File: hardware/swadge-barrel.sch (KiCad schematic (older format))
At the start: 42 parts, among them J1 USB_B_Micro, SW1 4-1437565-2, SW2 4-1437565-2, SW3 4-1437565-2, SW4 SW_SPDT, U1 ESP-13-WROOM-02D, U2 DISP_OLED_UG-2864HSWEG01, U3 BUS_PCIexpress, U4 QMA6981, U5 AP1117-33

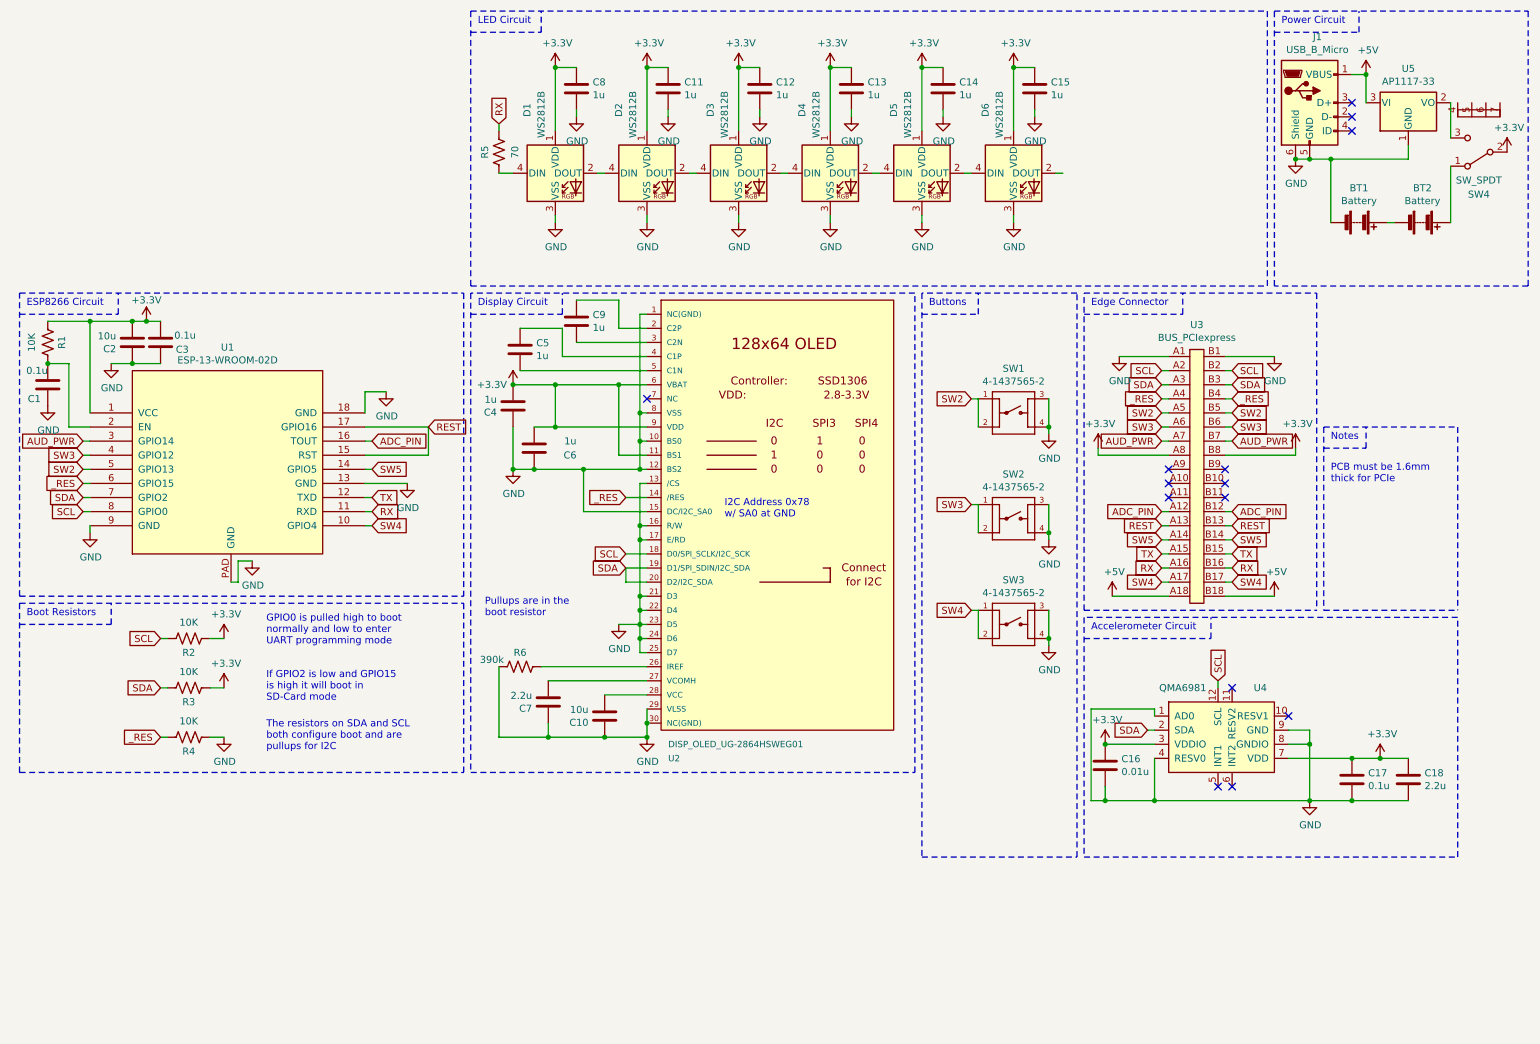
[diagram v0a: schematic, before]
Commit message: Added 12mm buttons
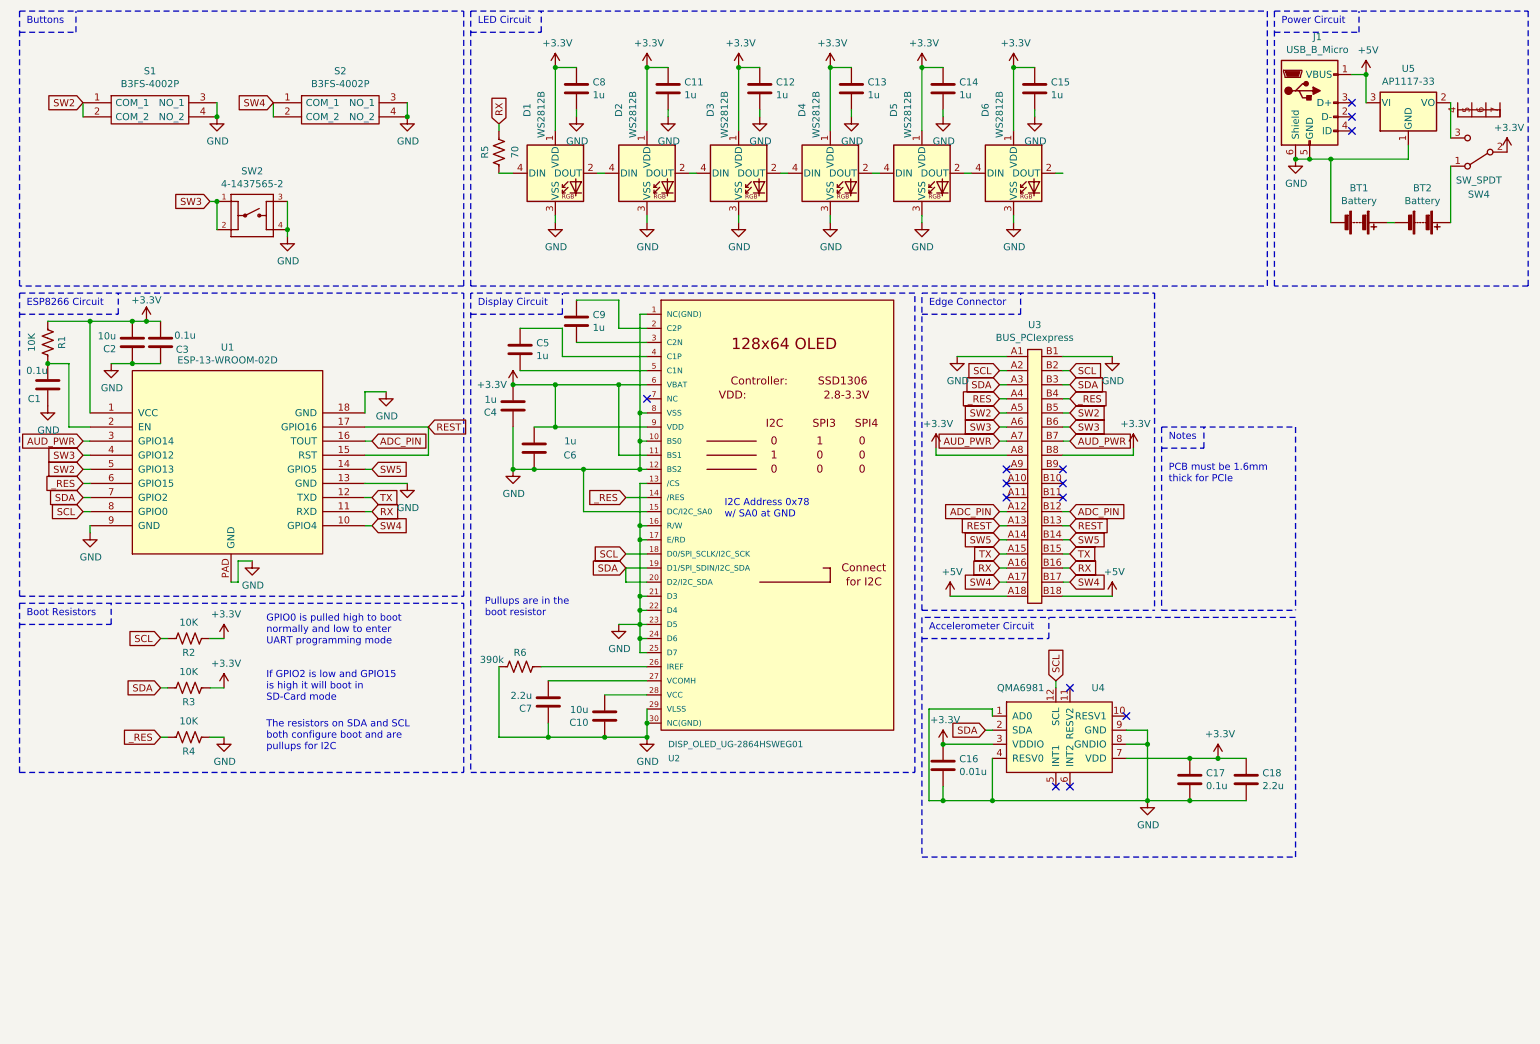
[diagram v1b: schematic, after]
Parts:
- removed SW1, SW3: 4-1437565-2, Swadge_Parts:SW_4-1437565-2, symbol Swadge_Parts:4-1437565-2
- added S1, S2: B3FS-4002P, Swadge_Parts:B3FS4002P, symbol Swadge_Parts:B3FS-4002P
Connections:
- net GND: now also S1.3 (NO_1), S1.4 (NO_2), S2.3 (NO_1), S2.4 (NO_2)
- net SW2: now also S1.1 (COM_1), S1.2 (COM_2)
- net SW4: now also S2.1 (COM_1), S2.2 (COM_2)
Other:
- moved on the sheet: C16, C17, C18, SW2, U3, U4

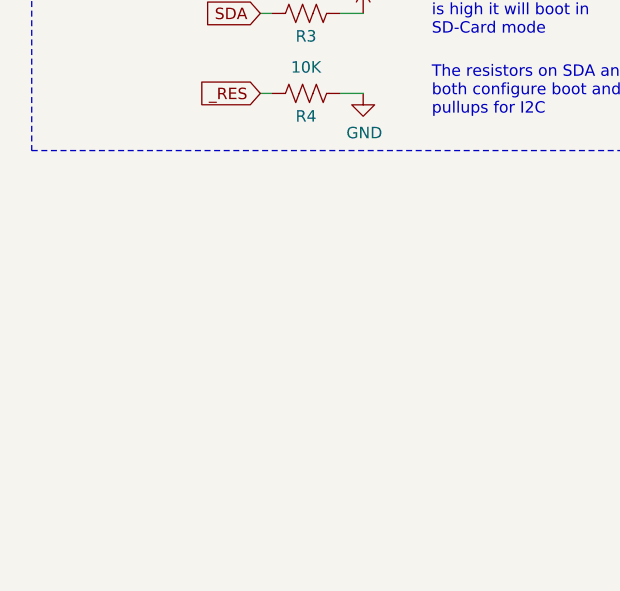
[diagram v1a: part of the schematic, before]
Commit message: Added THT buzzer to barrel board
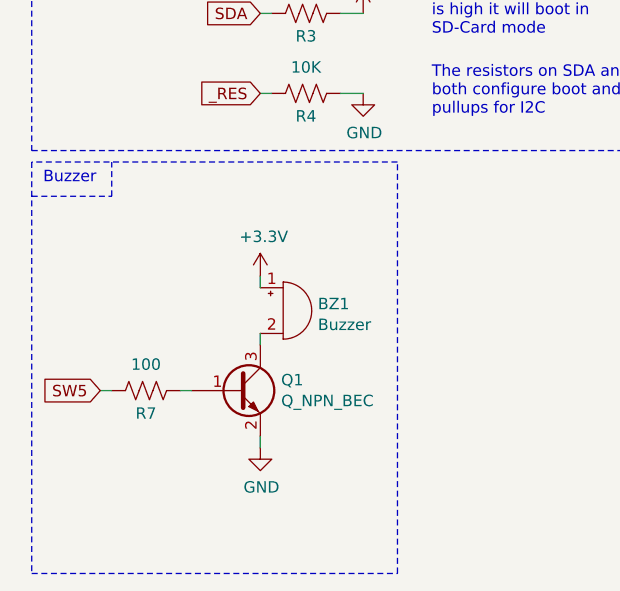
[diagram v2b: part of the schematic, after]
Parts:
- added BZ1: Buzzer, Swadge_Parts:Buzzer_12x9.5RM7.6, symbol Swadge_Parts:Buzzer
- added Q1: Q_NPN_BEC, Swadge_Parts:SOT-23, symbol Swadge_Parts:Q_NPN_BEC
- added R7: 100, Swadge_Parts:R_0603_1608Metric, symbol Swadge_Parts:R_US
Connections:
- net +3V3: now also BZ1.1 (-)
- net GND: now also Q1.2 (E)
- net SW5: now also R7.2
- new net: BZ1.2 (+), Q1.3 (C)
- new net: Q1.1 (B), R7.1
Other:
- note added: "Buzzer"
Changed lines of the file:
@@
 EESchema Schematic File Version 4
+LIBS:swadge-barrel-cache
 EELAYER 29 0
 EELAYER END
@@
 Wire Notes Line
 	3650 500  3650 2450
+$Comp
+L Swadge_Parts:Buzzer BZ1
+U 1 1 5D5EB51A
+P 1600 6600
+F 0 "BZ1" H 1752 6629 50  0000 L CNN
+F 1 "Buzzer" H 1752 6538 50  0000 L CNN
+F 2 "Swadge_Parts:Buzzer_12x9.5RM7.6" H 1850 6950 50  0001 C CNN
+F 3 "https://www.aliexpress.com/item/33004601553.html?spm=a2g0s.9042311.0.0.56834c4diZwZhE" V 1575 6700 50  0001 C CNN
+F 4 "433-1285-ND" H 1950 7050 50  0001 C CNN "Digikey"
+F 5 "49" H 1850 6850 50  0001 C CNN "Cost100"
+F 6 "Y" H 1850 7150 50  0001 C CNN "Substitutable"
+	1    1600 6600
+	1    0    0    -1
+$EndComp
+$Comp
+L Swadge_Parts:Q_NPN_BEC Q1
+U 1 1 5D5EC406
+P 1400 6950
+F 0 "Q1" H 1591 6996 50  0000 L CNN
+F 1 "Q_NPN_BEC" H 1591 6905 50  0000 L CNN
+F 2 "Swadge_Parts:SOT-23" H 2050 7300 50  0001 C CNN
+F 3 "https://www.onsemi.com/pub/Collateral/BC846ALT1-D.PDF" H 1400 6950 50  0001 C CNN
+F 4 "BC848BLT3GOSTR-ND" H 2050 7200 50  0001 C CNN "Digikey"
+F 5 "1.554" H 1750 7400 50  0001 C CNN "Cost100"
+F 6 "Y" H 1700 7500 50  0001 C CNN "Substitutable"
+	1    1400 6950
+	1    0    0    -1
+$EndComp
+$Comp
+L power:+3.3V #PWR033
+U 1 1 5D5EE737
+P 1500 6450
+F 0 "#PWR033" H 1500 6300 50  0001 C CNN
+F 1 "+3.3V" H 1515 6623 50  0000 C CNN
+F 2 "" H 1500 6450 50  0001 C CNN
+F 3 "" H 1500 6450 50  0001 C CNN
+	1    1500 6450
+	1    0    0    -1
+$EndComp
+Text GLabel 800  6950 0    50   Input ~ 0
+SW5
+Wire Wire Line
+	1150 6950 1200 6950
+$Comp
+L power:GND #PWR048
+U 1 1 5D5FD0B6
+P 1500 7200
+F 0 "#PWR048" H 1500 6950 50  0001 C CNN
+F 1 "GND" H 1505 7027 50  0000 C CNN
+F 2 "" H 1500 7200 50  0001 C CNN
+F 3 "" H 1500 7200 50  0001 C CNN
+	1    1500 7200
+	1    0    0    -1
+$EndComp
+Wire Wire Line
+	1500 7150 1500 7200
+$Comp
+L Swadge_Parts:R_US R7
+U 1 1 5D60B5AD
+P 1000 6950
+F 0 "R7" V 1100 6950 50  0000 C CNN
+F 1 "100" V 886 6950 50  0000 C CNN
+F 2 "Swadge_Parts:R_0603_1608Metric" V 1040 6940 50  0001 C CNN
+F 3 "" H 1000 6950 50  0001 C CNN
+F 4 "10" H -700 1300 50  0001 C CNN "Cost100"
+F 5 "RNCP0603FTD10K0CT-ND" H -700 1300 50  0001 C CNN "Digikey"
+F 6 "Y" H -700 1300 50  0001 C CNN "Substitutable"
+	1    1000 6950
+	0    1    1    0
+$EndComp
+Wire Wire Line
+	800  6950 850  6950
+Wire Wire Line
+	1500 6450 1500 6500
+Wire Wire Line
+	1500 6700 1500 6750
+Wire Notes Line
+	500  5950 500  7750
+Wire Notes Line
+	500  7750 2100 7750
+Wire Notes Line
+	2100 7750 2100 5950
+Wire Notes Line
+	2100 5950 500  5950
+Text Notes 550  6050 0    50   ~ 0
+Buzzer
+Wire Notes Line
+	500  6100 850  6100
+Wire Notes Line
+	850  6100 850  5950
 $EndSCHEMATC

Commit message: Routed board and lots of other things
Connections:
- net GND: now also SW4.4 (D), SW4.5 (E), SW4.6 (F), SW4.7 (G)
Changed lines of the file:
@@
 	9650 1550 9550 1550
 NoConn ~ 9950 1350
-$Comp
-L Swadge_Parts:SW_SPDT SW4
-U 1 1 5C3F7306
-P 10850 1500
-F 0 "SW4" H 10850 1800 50  0000 C CNN
-F 1 "SW_SPDT" H 10850 1700 50  0000 C CNN
-F 2 "Swadge_Parts:SW_SPDT_PCM12" H 10850 1500 50  0001 C CNN
-F 3 "https://www.ckswitches.com/media/1424/pcm.pdf" H 10850 1500 50  0001 C CNN
-F 4 "96" H 0   0   50  0001 C CNN "Cost100"
-F 5 "401-2016-1-ND" H 0   0   50  0001 C CNN "Digikey"
-F 6 "Y" H 0   0   50  0001 C CNN "Substitutable"
-	1    10850 1500
-	-1   0    0    1
-$EndComp
 Connection ~ 9650 1550
 $Comp
@@
 Wire Notes Line
 	850  6100 850  5950
+$Comp
+L power:GND #PWR0102
+U 1 1 5D73519E
+P 11000 1000
+F 0 "#PWR0102" H 11000 750 50  0001 C CNN
+F 1 "GND" H 11005 827 50  0000 C CNN
+F 2 "" H 11000 1000 50  0001 C CNN
+F 3 "" H 11000 1000 50  0001 C CNN
+	1    11000 1000
+	1    0    0    -1
+$EndComp
+$Comp
+L Swadge_Parts:SW_SPDT SW4
+U 1 1 5C3F7306
+P 10850 1500
+F 0 "SW4" H 10850 1800 50  0000 C CNN
+F 1 "SW_SPDT" H 10850 1700 50  0000 C CNN
+F 2 "Swadge_Parts:SW_SPDT_PCM12" H 10850 1500 50  0001 C CNN
+F 3 "https://www.ckswitches.com/media/1424/pcm.pdf" H 10850 1500 50  0001 C CNN
+F 4 "96" H 0   0   50  0001 C CNN "Cost100"
+F 5 "401-2016-1-ND" H 0   0   50  0001 C CNN "Digikey"
+F 6 "Y" H 0   0   50  0001 C CNN "Substitutable"
+	1    10850 1500
+	-1   0    0    1
+$EndComp
+Wire Wire Line
+	10700 1150 10800 1150
+Wire Wire Line
+	10900 1150 10800 1150
+Connection ~ 10800 1150
+Wire Wire Line
+	10900 1150 11000 1150
+Connection ~ 10900 1150
+Wire Wire Line
+	10800 1150 10800 1000
+Wire Wire Line
+	10800 1000 11000 1000
 $EndSCHEMATC

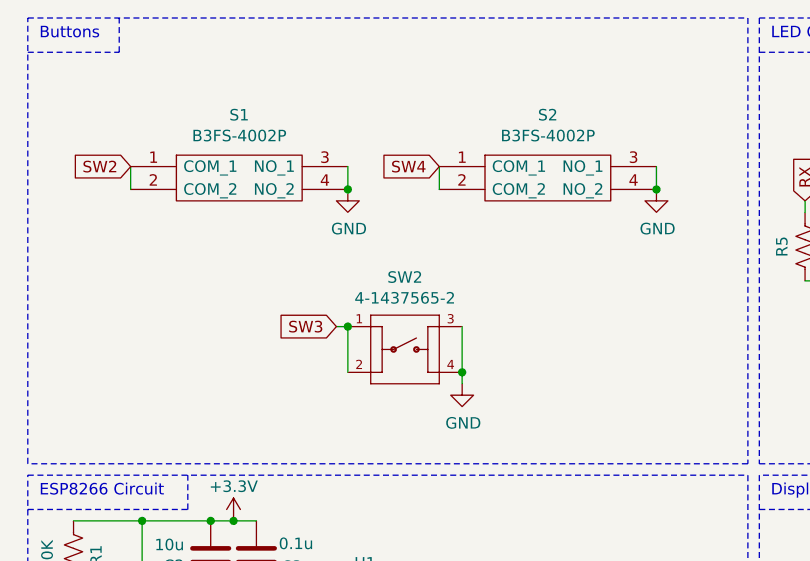
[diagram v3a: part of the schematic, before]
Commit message: Now has a single hole
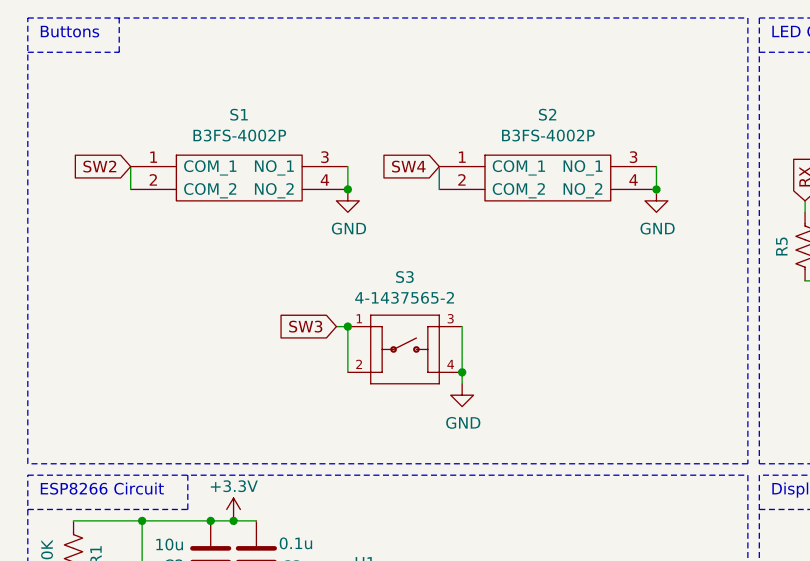
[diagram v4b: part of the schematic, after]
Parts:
- renumbered SW2 to S3
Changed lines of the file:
@@
 	10050 950  10050 1150
 $Comp
-L Swadge_Parts:4-1437565-2 SW2
+L Swadge_Parts:4-1437565-2 S3
 U 1 1 5C53358A
 P 2150 1950
-F 0 "SW2" H 2150 2265 50  0000 C CNN
+F 0 "S3" H 2150 2265 50  0000 C CNN
 F 1 "4-1437565-2" H 2150 2174 50  0000 C CNN
 F 2 "Swadge_Parts:SW_4-1437565-2" H 2150 1950 50  0001 L BNN

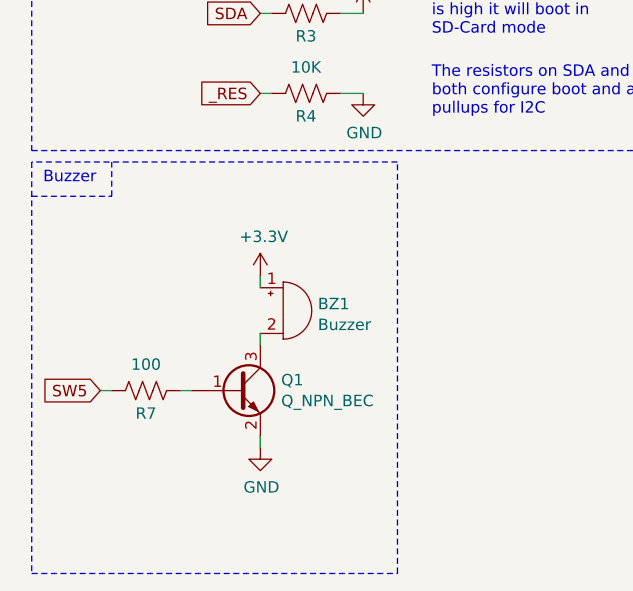
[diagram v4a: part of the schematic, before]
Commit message: Moved a lot of silk to F.Fab. Updated buzzer footprint
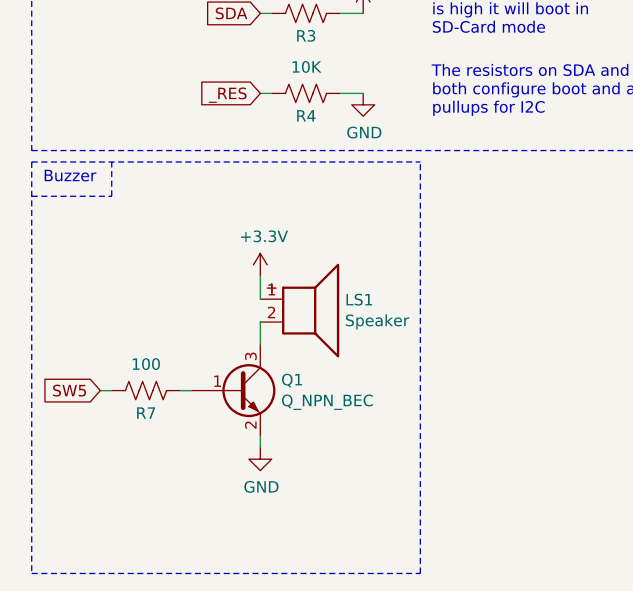
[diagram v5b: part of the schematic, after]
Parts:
- removed BZ1: Buzzer, Swadge_Parts:Buzzer_12x9.5RM7.6, symbol Swadge_Parts:Buzzer
- added LS1: Speaker, Swadge_Parts:Speaker_9mm, symbol Swadge_Parts:Speaker
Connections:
- net +3V3: now also LS1.1
- net at Q1.3 (C): now also LS1.2
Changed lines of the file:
@@
 	3650 500  3650 2450
-$Comp
-L Swadge_Parts:Buzzer BZ1
-U 1 1 5D5EB51A
-P 1600 6600
-F 0 "BZ1" H 1752 6629 50  0000 L CNN
-F 1 "Buzzer" H 1752 6538 50  0000 L CNN
-F 2 "Swadge_Parts:Buzzer_12x9.5RM7.6" H 1850 6950 50  0001 C CNN
-F 3 "https://www.aliexpress.com/item/33004601553.html?spm=a2g0s.9042311.0.0.56834c4diZwZhE" V 1575 6700 50  0001 C CNN
-F 4 "433-1285-ND" H 1950 7050 50  0001 C CNN "Digikey"
-F 5 "49" H 1850 6850 50  0001 C CNN "Cost100"
-F 6 "Y" H 1850 7150 50  0001 C CNN "Substitutable"
-	1    1600 6600
-	1    0    0    -1
-$EndComp
 $Comp
 L Swadge_Parts:Q_NPN_BEC Q1
@@
 Wire Wire Line
 	800  6950 850  6950
-Wire Wire Line
-	1500 6450 1500 6500
-Wire Wire Line
-	1500 6700 1500 6750
 Wire Notes Line
 	500  5950 500  7750
 Wire Notes Line
-	500  7750 2100 7750
-Wire Notes Line
-	2100 7750 2100 5950
-Wire Notes Line
-	2100 5950 500  5950
+	2200 7750 2200 5950
 Text Notes 550  6050 0    50   ~ 0
 Buzzer
@@
 Wire Wire Line
 	10800 1000 11000 1000
+$Comp
+L Swadge_Parts:Speaker LS1
+U 1 1 5D6E9B01
+P 1700 6550
+F 0 "LS1" H 1870 6546 50  0000 L CNN
+F 1 "Speaker" H 1870 6455 50  0000 L CNN
+F 2 "Swadge_Parts:Speaker_9mm" H 1700 6350 50  0001 C CNN
+F 3 "https://datasheet.lcsc.com/szlcsc/Jiangsu-Huaneng-Elec-HNB09A03_C96102.pdf" H 1690 6500 50  0001 C CNN
+F 4 "https://lcsc.com/product-detail/Buzzers_Jiangsu-Huaneng-Elec-HNB09A03_C96102.html" H 1300 6900 50  0001 C CNN "Digikey"
+F 5 "13.48" H 1950 6800 50  0001 C CNN "Cost100"
+F 6 "Y" H 1950 7050 50  0001 C CNN "Substitutable"
+	1    1700 6550
+	1    0    0    -1
+$EndComp
+Wire Wire Line
+	1500 6650 1500 6750
+Wire Wire Line
+	1500 6450 1500 6550
+Wire Notes Line
+	500  5950 2200 5950
+Wire Notes Line
+	500  7750 2200 7750
 $EndSCHEMATC
